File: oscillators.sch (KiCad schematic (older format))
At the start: 136 parts, among them Q29 MMBF4391LT1G, Q30 MMBF4391LT1G, Q31 2SC4207, Q32 2SC4207, Q33 PMBT2369, Q34 PMBT2369, Q35 2SA1832, Q36 2SA1832, Q37 PMBT2369, Q38 2SC4738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

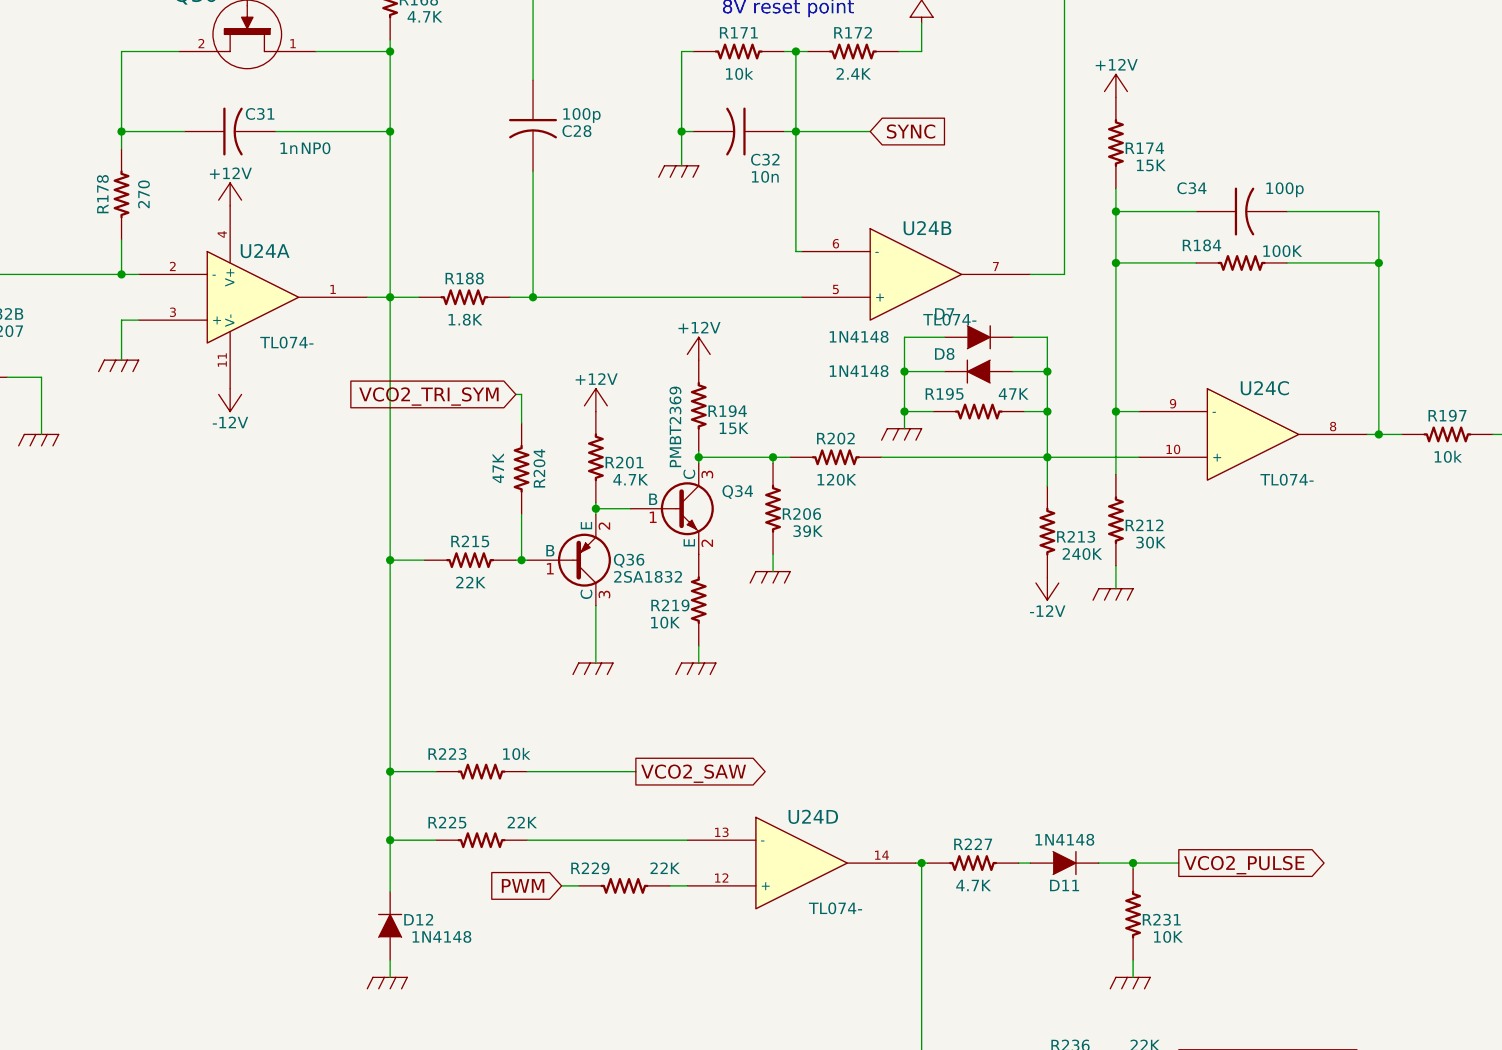
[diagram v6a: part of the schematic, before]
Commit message: more VCO2 placement
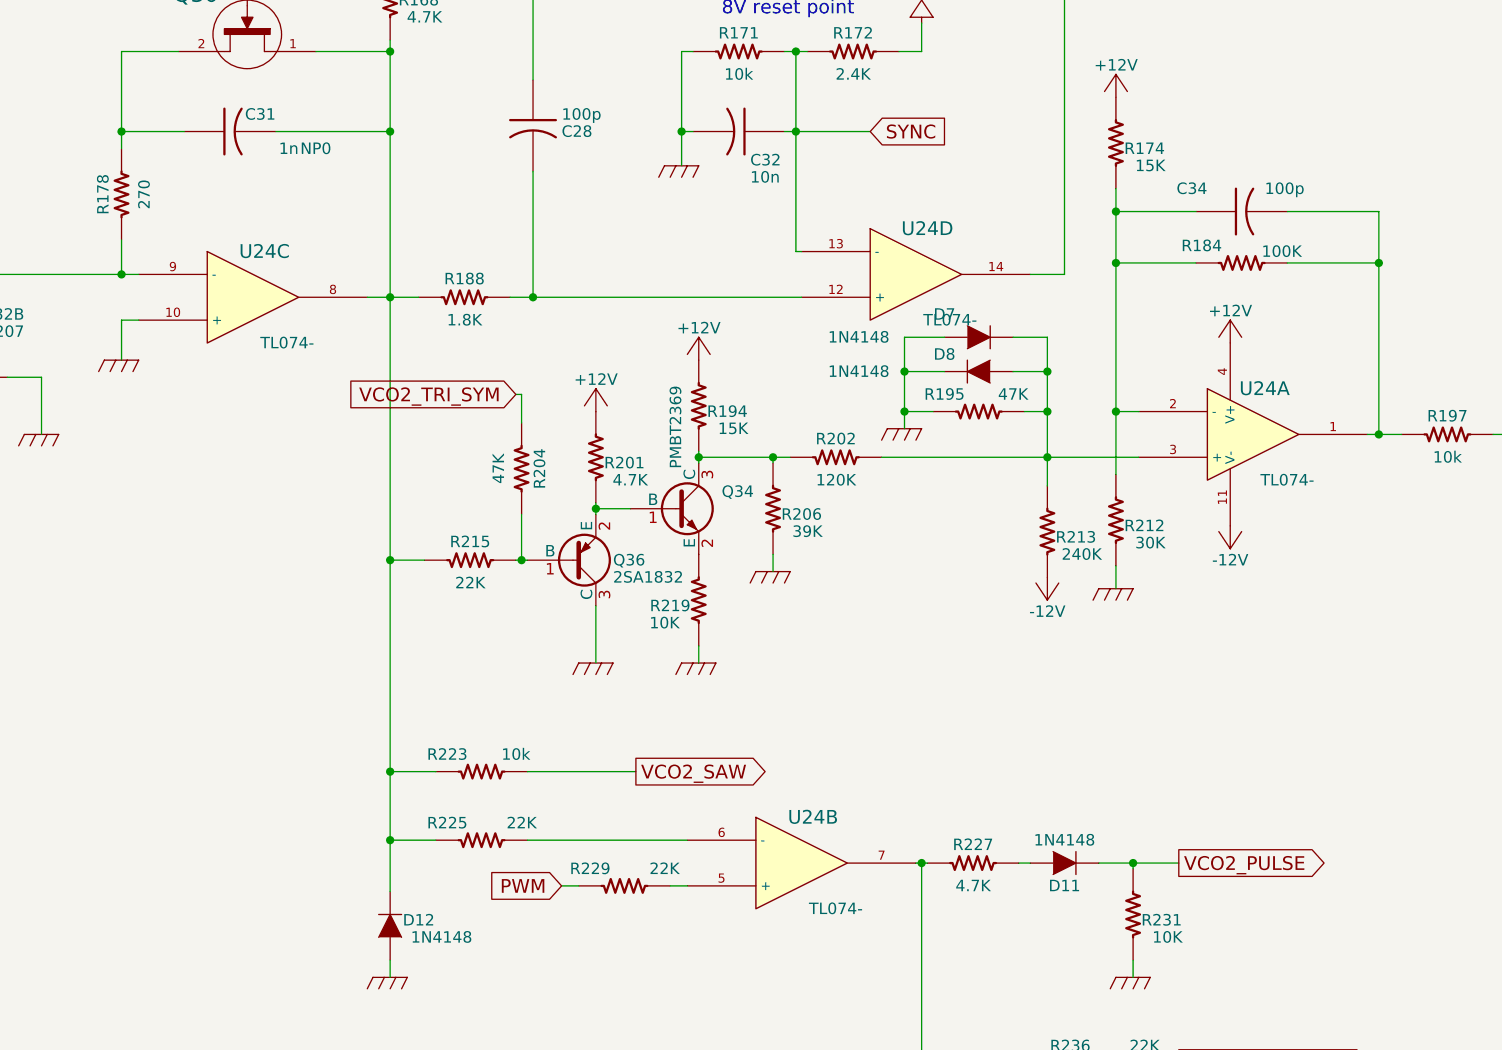
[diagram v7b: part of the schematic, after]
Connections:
- net GND: now also U24.10 (+); no longer U24.3 (+)
- net SYNC: now also U24.13 (-); no longer U24.6 (-)
- net at C31.2, D12.1 (K), Q30.1 (D)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: now also U24.8; no longer U24.1
- net at Q32.4 (C), R178.1: now also U24.9 (-); no longer U24.2 (-)
- net at C28.1, D6.1 (K): now also U24.14; no longer U24.7
- net at C28.2, R188.2: now also U24.12 (+); no longer U24.5 (+)
- net at C34.1, R174.1, R184.1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: now also U24.2 (-); no longer U24.9 (-)
- net at C34.2, R184.2, R197.1: now also U24.1; no longer U24.8
- net at R227.1, R236.1: now also U24.7; no longer U24.14
- net at R225.2: now also U24.6 (-); no longer U24.13 (-)
- net at R229.2: now also U24.5 (+); no longer U24.12 (+)
- net at D7.1 (K), D8.2 (A), R195.2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: now also U24.3 (+); no longer U24.10 (+)
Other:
- moved on the sheet: U24A, U24B, U24C, U24D
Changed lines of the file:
@@
 L +12V #PWR0213
 U 1 1 5819C732
-P 22375 7500
-F 0 "#PWR0213" H 22375 7350 50  0001 C CNN
-F 1 "+12V" H 22375 7640 50  0000 C CNN
-F 2 "" H 22375 7500 60  0000 C CNN
-F 3 "" H 22375 7500 60  0000 C CNN
-	1    22375 7500
+P 26750 8100
+F 0 "#PWR0213" H 26750 7950 50  0001 C CNN
+F 1 "+12V" H 26750 8240 50  0000 C CNN
+F 2 "" H 26750 8100 60  0000 C CNN
+F 3 "" H 26750 8100 60  0000 C CNN
+	1    26750 8100
 	1    0    0    -1
 $EndComp
@@
 L -12V #PWR0214
 U 1 1 5819C738
-P 22375 8300
-F 0 "#PWR0214" H 22375 8400 30  0001 C CNN
-F 1 "-12V" H 22375 8450 50  0000 C CNN
-F 2 "~" H 22375 8300 60  0000 C CNN
-F 3 "~" H 22375 8300 60  0000 C CNN
-	1    22375 8300
+P 26750 8900
+F 0 "#PWR0214" H 26750 9000 30  0001 C CNN
+F 1 "-12V" H 26750 9050 50  0000 C CNN
+F 2 "~" H 26750 8900 60  0000 C CNN
+F 3 "~" H 26750 8900 60  0000 C CNN
+	1    26750 8900
 	-1   0    0    1
 $EndComp
@@
 L TL074- U24
 U 1 1 5A736F14
+P 26850 8500
+F 0 "U24" H 26900 8700 60  0000 C CNN
+F 1 "TL074-" H 27000 8300 50  0000 C CNN
+F 2 "Housings_SSOP:TSSOP-14_4.4x5mm_Pitch0.65mm" H 26850 8500 60  0001 C CNN
+F 3 "" H 26850 8500 60  0000 C CNN
+	1    26850 8500
+	1    0    0    -1
+$EndComp
+$Comp
+L TL074- U24
+U 2 1 5A737DEF
+P 24875 10375
+F 0 "U24" H 24925 10575 60  0000 C CNN
+F 1 "TL074-" H 25025 10175 50  0000 C CNN
+F 2 "Housings_SSOP:TSSOP-14_4.4x5mm_Pitch0.65mm" H 24875 10375 60  0001 C CNN
+F 3 "" H 24875 10375 60  0000 C CNN
+	2    24875 10375
+	1    0    0    -1
+$EndComp
+$Comp
+L TL074- U24
+U 4 1 5A738BF4
+P 25375 7800
+F 0 "U24" H 25425 8000 60  0000 C CNN
+F 1 "TL074-" H 25525 7600 50  0000 C CNN
+F 2 "Housings_SSOP:TSSOP-14_4.4x5mm_Pitch0.65mm" H 25375 7800 60  0001 C CNN
+F 3 "" H 25375 7800 60  0000 C CNN
+	4    25375 7800
+	1    0    0    -1
+$EndComp
+$Comp
+L TL074- U24
+U 3 1 5A738F22
 P 22475 7900
 F 0 "U24" H 22525 8100 60  0000 C CNN
@@
 F 2 "Housings_SSOP:TSSOP-14_4.4x5mm_Pitch0.65mm" H 22475 7900 60  0001 C CNN
 F 3 "" H 22475 7900 60  0000 C CNN
-	1    22475 7900
-	1    0    0    -1
-$EndComp
-$Comp
-L TL074- U24
-U 2 1 5A737DEF
-P 25375 7800
-F 0 "U24" H 25425 8000 60  0000 C CNN
-F 1 "TL074-" H 25525 7600 50  0000 C CNN
-F 2 "Housings_SSOP:TSSOP-14_4.4x5mm_Pitch0.65mm" H 25375 7800 60  0001 C CNN
-F 3 "" H 25375 7800 60  0000 C CNN
-	2    25375 7800
-	1    0    0    -1
-$EndComp
-$Comp
-L TL074- U24
-U 4 1 5A738BF4
-P 24875 10375
-F 0 "U24" H 24925 10575 60  0000 C CNN
-F 1 "TL074-" H 25025 10175 50  0000 C CNN
-F 2 "Housings_SSOP:TSSOP-14_4.4x5mm_Pitch0.65mm" H 24875 10375 60  0001 C CNN
-F 3 "" H 24875 10375 60  0000 C CNN
-	4    24875 10375
-	1    0    0    -1
-$EndComp
-$Comp
-L TL074- U24
-U 3 1 5A738F22
-P 26850 8500
-F 0 "U24" H 26900 8700 60  0000 C CNN
-F 1 "TL074-" H 27000 8300 50  0000 C CNN
-F 2 "Housings_SSOP:TSSOP-14_4.4x5mm_Pitch0.65mm" H 26850 8500 60  0001 C CNN
-F 3 "" H 26850 8500 60  0000 C CNN
-	3    26850 8500
-	1    0    0    -1
-$EndComp
+	3    22475 7900
+	1    0    0    -1
+$EndComp
